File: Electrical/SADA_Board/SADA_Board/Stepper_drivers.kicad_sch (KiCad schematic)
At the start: 6 parts

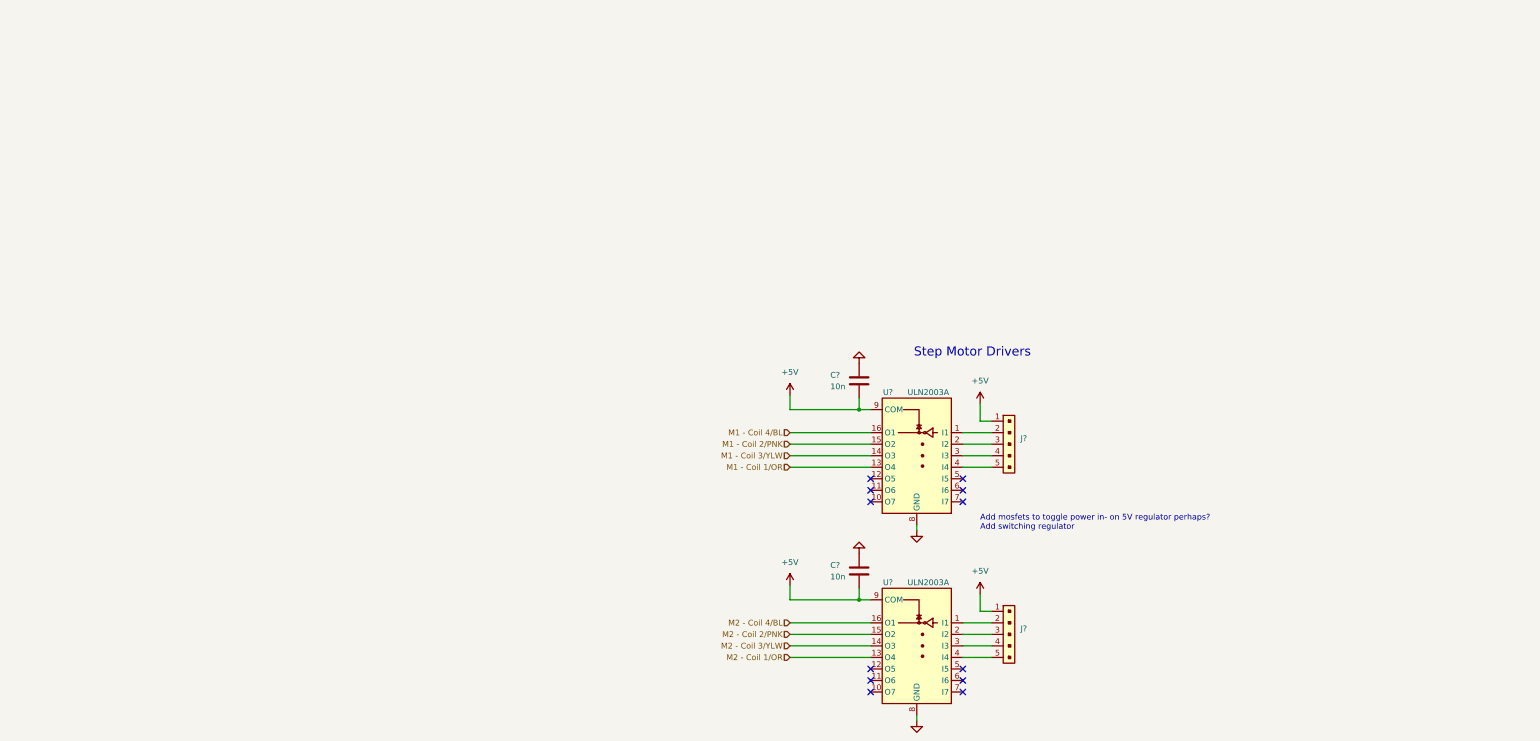
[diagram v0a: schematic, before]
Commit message: Partial implementation of stepper motor Step up
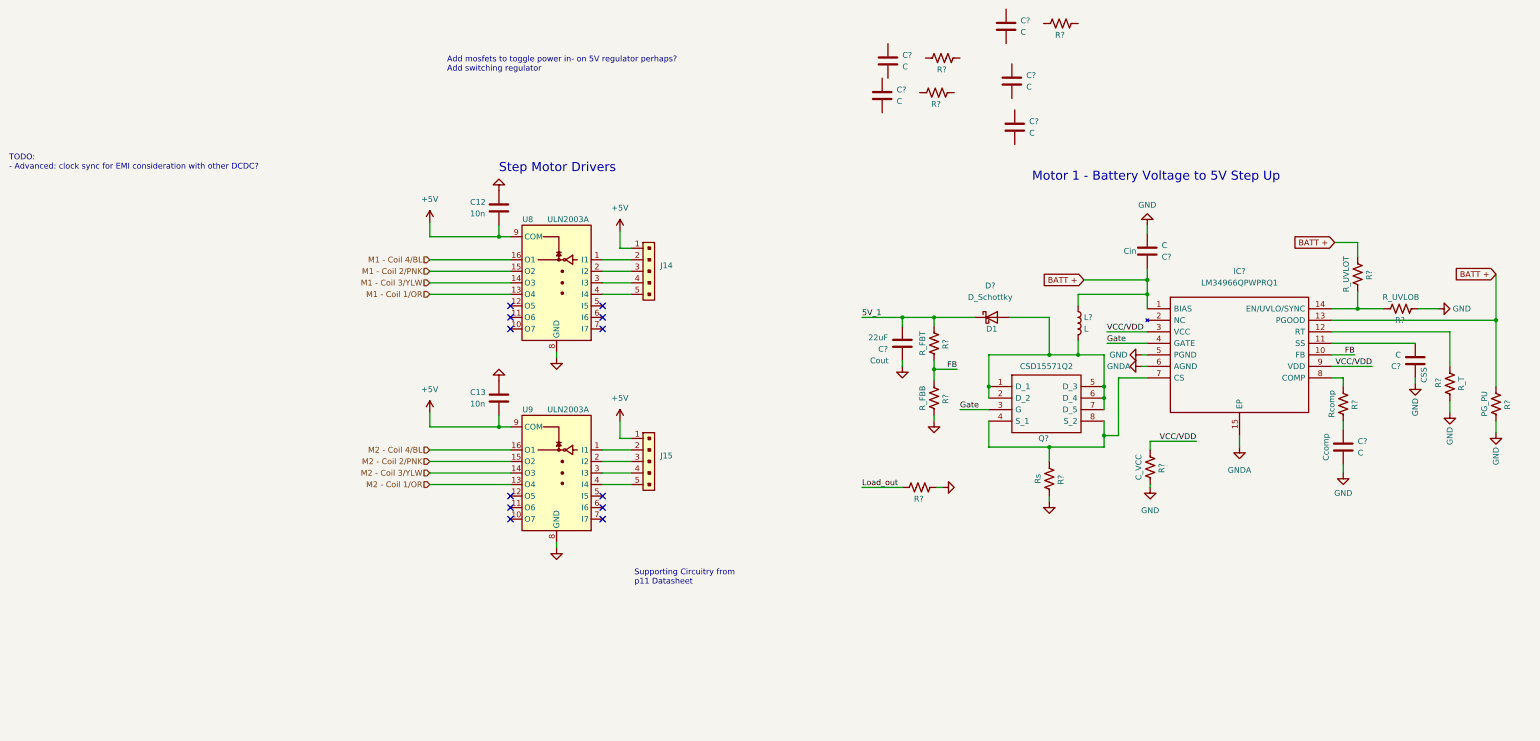
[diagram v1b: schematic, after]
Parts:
- added C? (x8): C, symbol Device:C
- added C?: 22uF, Capacitor_SMD:C_0805_2012Metric, symbol Device:C
- added D?: D_Schottky, symbol Device:D_Schottky
- added IC?: LM34966QPWPRQ1, SOP65P640X120-15N, symbol LM34966QPWPRQ1:LM34966QPWPRQ1
- added L?: L, symbol Device:L
- added Q?: CSD15571Q2, CSD15571Q2, symbol CSD15571Q2:CSD15571Q2
- added R?: 4.7k, Resistor_SMD:R_0201_0603Metric, symbol Device:R_US
- added R? (x9): R, symbol Device:R_US
- added R?: 10k, symbol Device:R_US
- added R?: 49.9k, Resistor_SMD:R_0201_0603Metric, symbol Device:R_US
- added R?: 18.7k, Resistor_SMD:R_0201_0603Metric, symbol Device:R_US
- gave numbers to parts that had none: 6
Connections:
- net GND: now also C?.1, C?.1, C?.2, C?.2, IC?.5 (PGND), R?.1, R?.1, R?.1, R?.2, R?.2, R?.2, R?.2
- new net: C?.1, R?.2
- new net: C?.2, IC?.11 (SS)
- new net: IC?.12 (RT), R?.2
- new net: IC?.14 (EN/UVLO/SYNC), R?.2, R?.2
- new net: IC?.7 (CS), Q?.4 (S_1), Q?.8 (S_2), R?.1
- new net: IC?.8 (COMP), R?.1
- new net: D?.2 (A), L?.2, Q?.1 (D_1), Q?.2 (D_2), Q?.5 (D_3), Q?.6 (D_4), Q?.7 (D_5)
- new net 5V_1: C?.2, D?.1 (K), R?.1
- new net BATT +: C?.1, IC?.1 (BIAS), IC?.13 (PGOOD), L?.1, R?.1, R?.1
- new net FB: IC?.10 (FB), R?.1, R?.2
- new net GNDA: IC?.15 (EP), IC?.6 (AGND)
- new net Gate: IC?.4 (GATE), Q?.3 (G)
- new net Load_out: R?.2
- new net VCC/VDD: IC?.3 (VCC), IC?.9 (VDD), R?.1
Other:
- note added: "Motor 1 - Battery Voltage to 5V Step Up"
- note added: "Supporting Circuitry from p11 Datasheet"
- note added: "TODO: - Advanced: clock sync for EMI consideration with other DCDC?"
- moved on the sheet: C12, C13, J14, J15, U8, U9

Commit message: Rough draft stepup done
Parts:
- removed R? (x3): R, symbol Device:R_US
- added R19: 10k, Resistor_SMD:R_0603_1608Metric, symbol Device:R_US
- C17: renamed from C?; value 22uF -> 15uF; footprint Capacitor_SMD:C_0805_2012Metric -> Capacitor_SMD:C_1210_3225Metric; MPN C2012X7S1A226M125AC -> CGA6P3X7R1C156M250AB
- C18: renamed from C?; value C -> 0.22 uF; footprint (none) -> Resistor_SMD:R_0201_0603Metric; MPN (none) -> CGA3E3X7R1H224K080AB
- C20: renamed from C?; value C -> 750pF; footprint (none) -> Capacitor_SMD:C_0402_1005Metric; MPN (none) -> GRM1555C1H751GA01D; Part (none) -> C_HF
- C21: renamed from C?; value C -> 1 uF; footprint (none) -> Resistor_SMD:R_0201_0603Metric; MPN (none) -> GCM188R71C105MA64D; Part (none) -> C_VCC
- C22: renamed from C?; value C -> 33nF; footprint (none) -> Capacitor_SMD:C_0805_2012Metric; MPN (none) -> CGA4J2C0G1H333J125AA
- D1: renamed from D?; footprint (none) -> Miles Added:DIOM5226X240N; MPN (none) -> VS-50WQ04FN-M3
- L1: renamed from L?; value L -> 3.3 uH; footprint (none) -> 0_custom:XAL1010-682MED; MPN (none) -> XAL1010-332MED
- R18: renamed from R?; value R -> 12k; footprint (none) -> Resistor_SMD:R_0603_1608Metric; MPN (none) -> RT0603BRD0713KL; Part (none) -> R_UVLOT
- R23: renamed from R?; value 10k -> 20k; footprint (none) -> Capacitor_SMD:C_0402_1005Metric; MPN (none) -> ERJ-U02J203X
- R24: renamed from R?; value R -> 2.55k; footprint (none) -> Capacitor_SMD:C_0402_1005Metric; MPN MPN -> RMCF0402FT2K55
- R25: renamed from R?; value R -> 0.04; footprint (none) -> Resistor_SMD:R_1206_3216Metric; MPN MPN -> TLRP2B10DR040FTD
- gave numbers to parts that had none: 12
- renumbered C12 to C15, C13 to C19, U9 to U10
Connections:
- net BATT +: now also R18.2
- net GND: now also C20.2, C21.2; no longer C18.1, R21.1, R22.2
- net GNDA: now also C18.1, R21.1, R22.2, R19.2
- net VCC/VDD: now also C21.1
- net at C20.1: now also R24.1, U9.8 (COMP)
- net at U9.14 (EN/UVLO/SYNC): now also R18.1, R19.1
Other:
- note added: "TODO: Add mosfets to toggle power in- on 5V regulator perhaps? Verify correct diode selection flyback diodes"
- note added: "Verify correct diode selection"
- note removed: "Add mosfets to toggle power in- on 5V regulator perhaps? Add switching regulator"
- note removed: "TODO: - Advanced: clock sync for EMI consideration with other DCDC?"
- moved on the sheet: C20, C21, C22, R18, R24

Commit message: Pre-regulator/bipolar stepper change
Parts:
- removed C15, C19: 10n, Capacitor_SMD:C_0805_2012Metric, symbol Device:C
- added C? (x2): 10n, Capacitor_SMD:C_0805_2012Metric, symbol Device:C
- added IC?: SQ3989EV-T1_GE3, SOT95P284X110-6N, symbol SQ3989EV-T1_GE3:SQ3989EV-T1_GE3
- added R?: 10k, Resistor_SMD:R_0402_1005Metric, symbol Device:R_US
- added R?: 100, Resistor_SMD:R_0402_1005Metric, symbol Device:R_US
- R20, R22: footprint Resistor_SMD:R_0201_0603Metric -> Resistor_SMD:R_0603_1608Metric
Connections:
- net 5V_1: now also J14.1, U8.9 (COM), C?.2, IC?.6 (D1); no longer C17.2, D1.1 (K), R20.1
- net GND: now also C?.1, C?.1
- net M1 - Coil 1/OR: now also U8.4 (I4); no longer U8.13 (O4)
- net M1 - Coil 2/PNK: now also U8.2 (I2); no longer U8.15 (O2)
- net M1 - Coil 3/YLW: now also U8.3 (I3); no longer U8.14 (O3)
- net M1 - Coil 4/BL: now also U8.1 (I1); no longer U8.16 (O1)
- net M2 - Coil 1/OR: now also U10.4 (I4); no longer U10.13 (O4)
- net M2 - Coil 2/PNK: now also U10.2 (I2); no longer U10.15 (O2)
- net M2 - Coil 3/YLW: now also U10.3 (I3); no longer U10.14 (O3)
- net M2 - Coil 4/BL: now also U10.1 (I1); no longer U10.16 (O1)
- net at J15.2: now also U10.16 (O1); no longer U10.1 (I1)
- net at J15.3: now also U10.15 (O2); no longer U10.2 (I2)
- net at J15.4: now also U10.14 (O3); no longer U10.3 (I3)
- net at J15.5: now also U10.13 (O4); no longer U10.4 (I4)
- net at J14.2: now also U8.16 (O1); no longer U8.1 (I1)
- net at J14.3: now also U8.15 (O2); no longer U8.2 (I2)
- net at J14.4: now also U8.14 (O3); no longer U8.3 (I3)
- net at J14.5: now also U8.13 (O4); no longer U8.4 (I4)
- net +5V renamed 5V_2
- net 5V_2: now also C?.2, IC?.4 (D2); no longer J14.1, U8.9 (COM)
- new net: IC?.1 (G1), IC?.3 (G2), R?.1, R?.1
- new net 5V_REG1_OUT: C17.2, D1.1 (K), IC?.2 (S2), IC?.5 (S1), R20.1, R?.2
- new net STP_TOGGLE: R?.2
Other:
- note added: "S20STH30-0604A"
- note added: "Schematic Notes: - ULN2003 has Internal Flyback Diodes"
- note added: "TODO: Add mosfets to toggle power in- on 5V regulator perhaps? Verify correct diode selection"
- note removed: "TODO: Add mosfets to toggle power in- on 5V regulator perhaps? Verify correct diode selection flyback diodes"
- moved on the sheet: C16, C17, C18, C20, C21, C22, D1, J14, J15, L1, Q1, R18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

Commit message: Connectors, Oscillator
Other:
- note removed: "S20STH30-0604A"
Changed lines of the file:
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@@
     (effects (font (size 2 2)) (justify left bottom))
-  )
-  (text " S20STH30-0604A" (at 189.865 140.335 0)
-    (effects (font (size 1.27 1.27)) (justify left bottom))
   )
   (text "Schematic Notes:\n- ULN2003 has Internal Flyback Diodes"
